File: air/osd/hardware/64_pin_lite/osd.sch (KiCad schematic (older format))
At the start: 0 parts

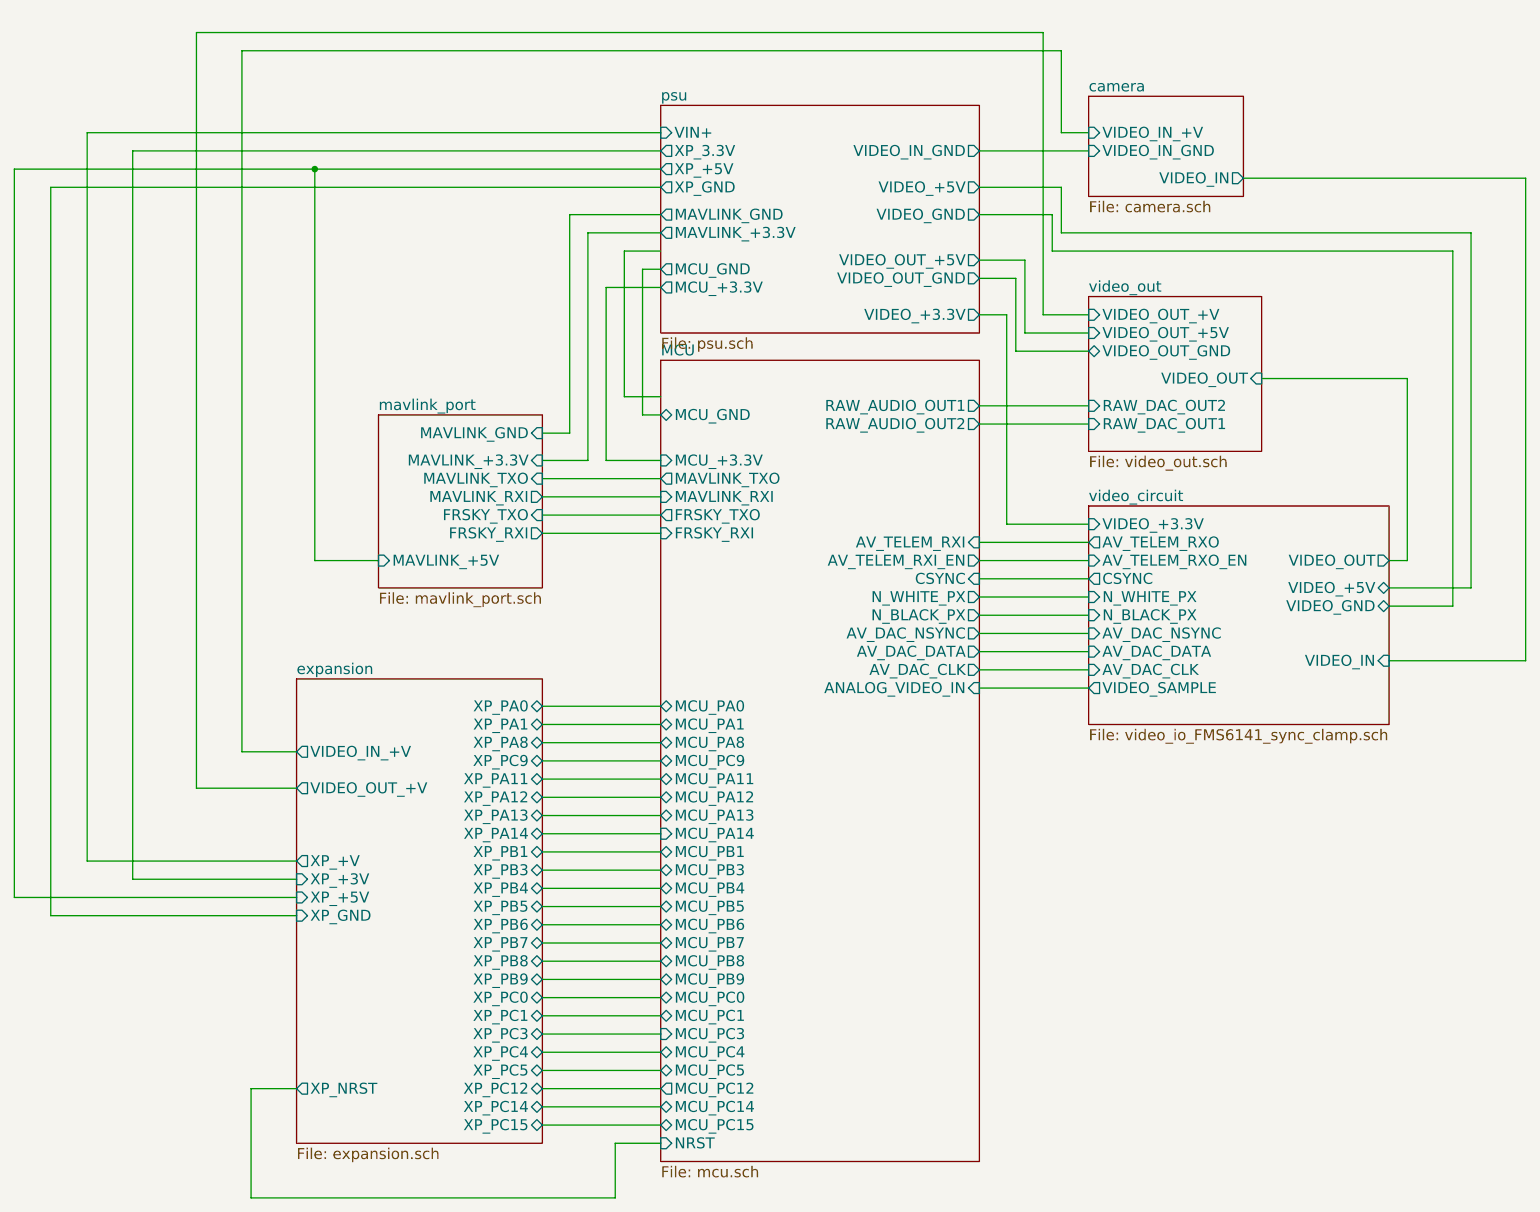
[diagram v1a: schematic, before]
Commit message: removed traces on pcb design. Added links to separate ground paths for modules. Moved mpu to other side of board. Added 2 pin power conector at end of board
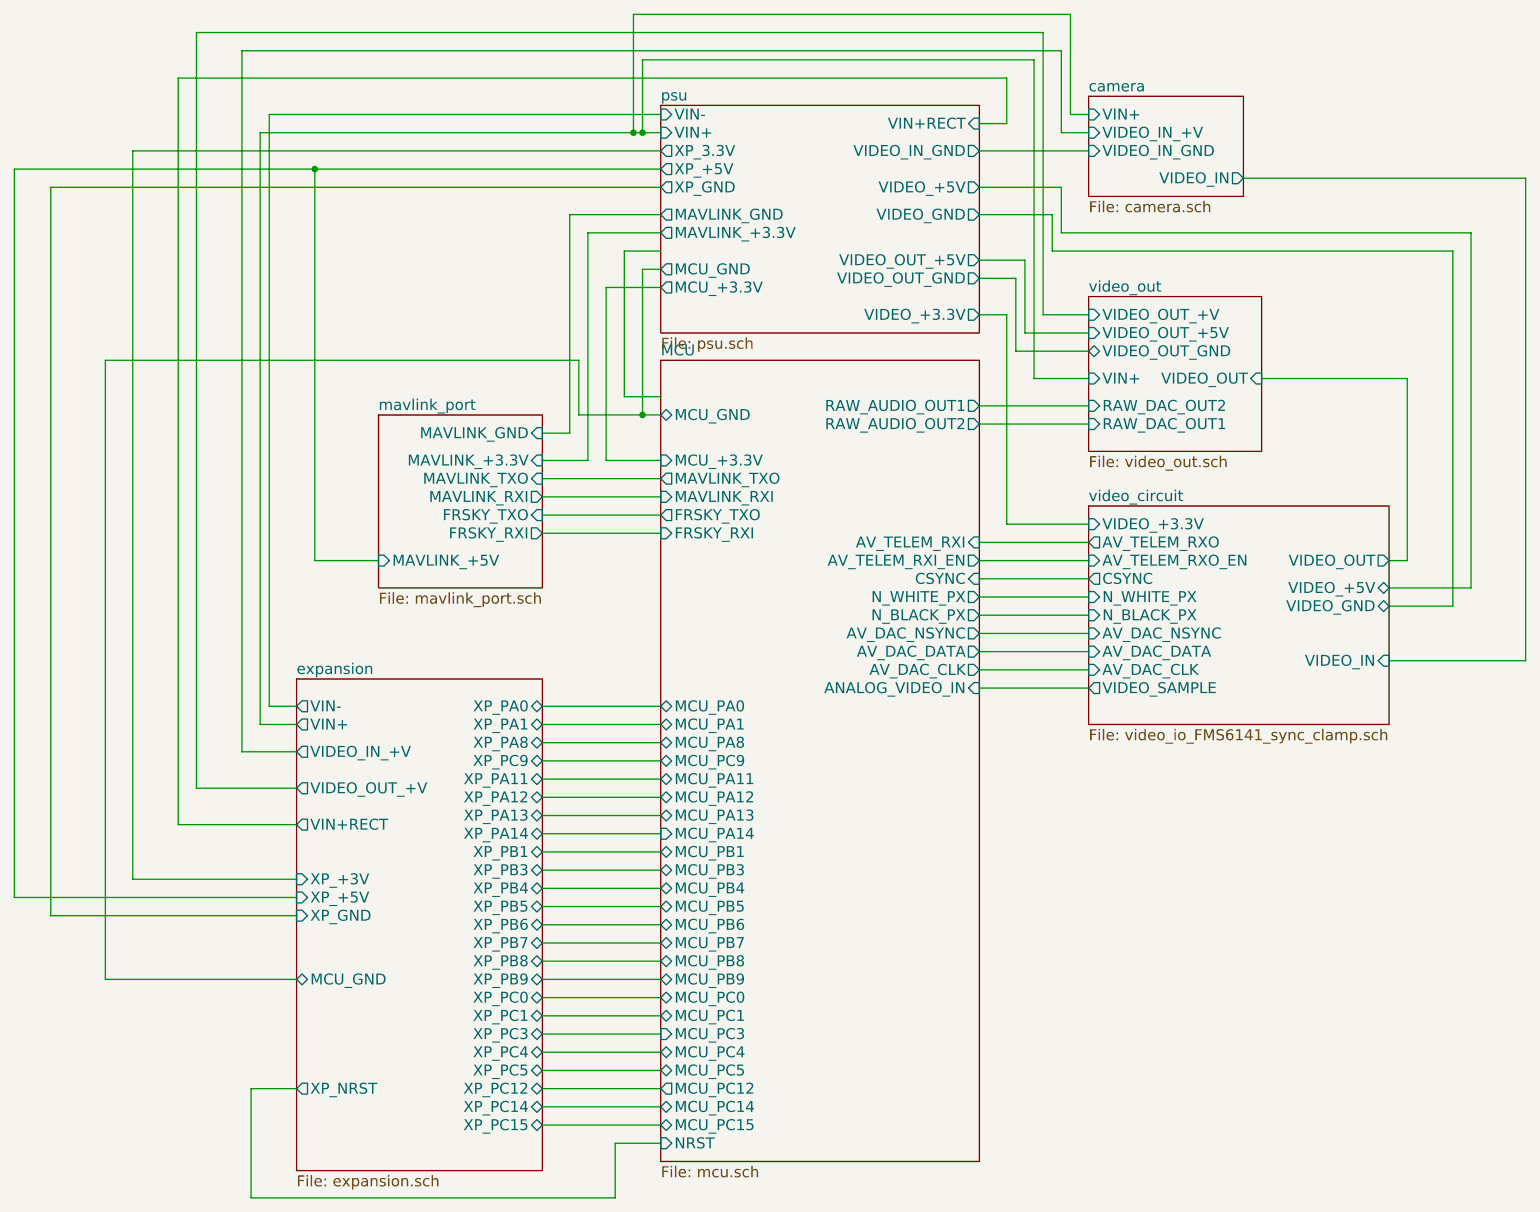
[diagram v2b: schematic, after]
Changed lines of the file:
@@
-EESchema Schematic File Version 2  date Mon 26 Jan 2015 12:32:55 GMT
+EESchema Schematic File Version 2  date Wed 04 Mar 2015 21:55:30 GMT
 LIBS:lm358
 LIBS:conn_6
@@
 LIBS:tlv3501
 LIBS:74lvc1g86
+LIBS:R0link
+LIBS:osd-cache
 EELAYER 25  0
 EELAYER END
@@
 Sheet 1 8
 Title ""
-Date "26 jan 2015"
+Date "4 mar 2015"
 Rev ""
 Comp ""
@@
 Comment4 ""
 $EndDescr
+Connection ~ 4600 1250
+Wire Wire Line
+	4600 1250 4600 850
+Wire Wire Line
+	4600 850  6750 850
+Wire Wire Line
+	6750 850  6750 2600
+Wire Wire Line
+	6750 2600 7050 2600
+Connection ~ 4600 2800
+Wire Wire Line
+	4700 2800 4250 2800
+Wire Wire Line
+	4250 2800 4250 2500
+Wire Wire Line
+	4250 2500 1650 2500
+Wire Wire Line
+	1650 2500 1650 5900
+Wire Wire Line
+	1650 5900 2700 5900
+Wire Wire Line
+	6450 1200 6600 1200
+Wire Wire Line
+	6600 1200 6600 950
+Wire Wire Line
+	6600 950  2050 950
+Wire Wire Line
+	2050 950  2050 5050
+Wire Wire Line
+	2050 5050 2700 5050
 Connection ~ 2800 1450
 Wire Wire Line
@@
 	4050 6700 4700 6700
 Wire Wire Line
-	4700 2800 4600 2800
-Wire Wire Line
 	4600 2800 4600 2000
 Wire Wire Line
@@
 	6450 2850 7050 2850
 Wire Wire Line
-	2700 5250 1550 5250
-Wire Wire Line
-	1550 5250 1550 1250
-Wire Wire Line
-	1550 1250 4700 1250
-Wire Wire Line
 	2700 4650 2400 4650
 Wire Wire Line
@@
 Wire Wire Line
 	4450 6800 4700 6800
+Wire Wire Line
+	2700 4400 2550 4400
+Wire Wire Line
+	2550 4400 2550 1150
+Wire Wire Line
+	2550 1150 4700 1150
+Wire Wire Line
+	2700 4500 2500 4500
+Wire Wire Line
+	2500 4500 2500 1250
+Wire Wire Line
+	2500 1250 4700 1250
+Wire Wire Line
+	7050 1150 6950 1150
+Wire Wire Line
+	6950 1150 6950 600
+Wire Wire Line
+	6950 600  4550 600
+Wire Wire Line
+	4550 600  4550 1250
+Connection ~ 4550 1250
 $Sheet
 S 4700 2500 1750 4400
@@
 F14 "MCU_+3.3V" O L 4700 2100 60
 F15 "XP_3.3V" O L 4700 1350 60
+F16 "VIN-" I L 4700 1150 60
+F17 "VIN+RECT" I R 6450 1200 60
 $EndSheet
 $Sheet
@@
 F3 "VIDEO_IN_GND" I L 7050 1350 60
 F4 "VIDEO_IN_+V" I L 7050 1250 60
-$EndSheet
-$Sheet
-S 2700 4250 1350 2550
+F5 "VIN+" I L 7050 1150 60
+$EndSheet
+$Sheet
+S 2700 4250 1350 2700
 U 546D98A5
 F0 "expansion" 60
@@
 F26 "XP_+5V" I L 2700 5450 60
 F27 "XP_PC12" B R 4050 6500 60
-F28 "XP_+V" O L 2700 5250 60
-F29 "XP_+3V" I L 2700 5350 60
-F30 "VIDEO_OUT_+V" O L 2700 4850 60
-F31 "VIDEO_IN_+V" O L 2700 4650 60
-F32 "XP_NRST" O L 2700 6500 60
+F28 "XP_+3V" I L 2700 5350 60
+F29 "VIDEO_OUT_+V" O L 2700 4850 60
+F30 "VIDEO_IN_+V" O L 2700 4650 60
+F31 "XP_NRST" O L 2700 6500 60
+F32 "VIN-" O L 2700 4400 60
+F33 "VIN+" O L 2700 4500 60
+F34 "VIN+RECT" O L 2700 5050 60
+F35 "MCU_GND" B L 2700 5900 60
 $EndSheet
 $Sheet
@@
 F6 "VIDEO_OUT_+5V" I L 7050 2350 60
 F7 "VIDEO_OUT_+V" I L 7050 2250 60
-$EndSheet
-$Sheet
+F8 "VIN+" I L 7050 2600 60
+$EndSheet
+$Sheet

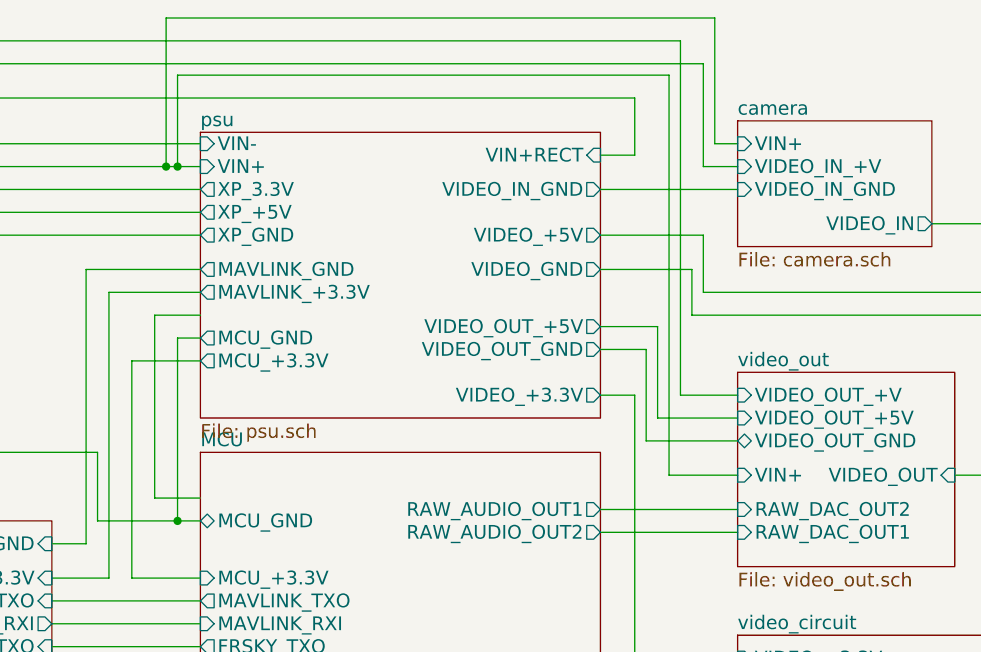
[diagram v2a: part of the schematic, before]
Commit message: laid out components on boar. No traces done yet
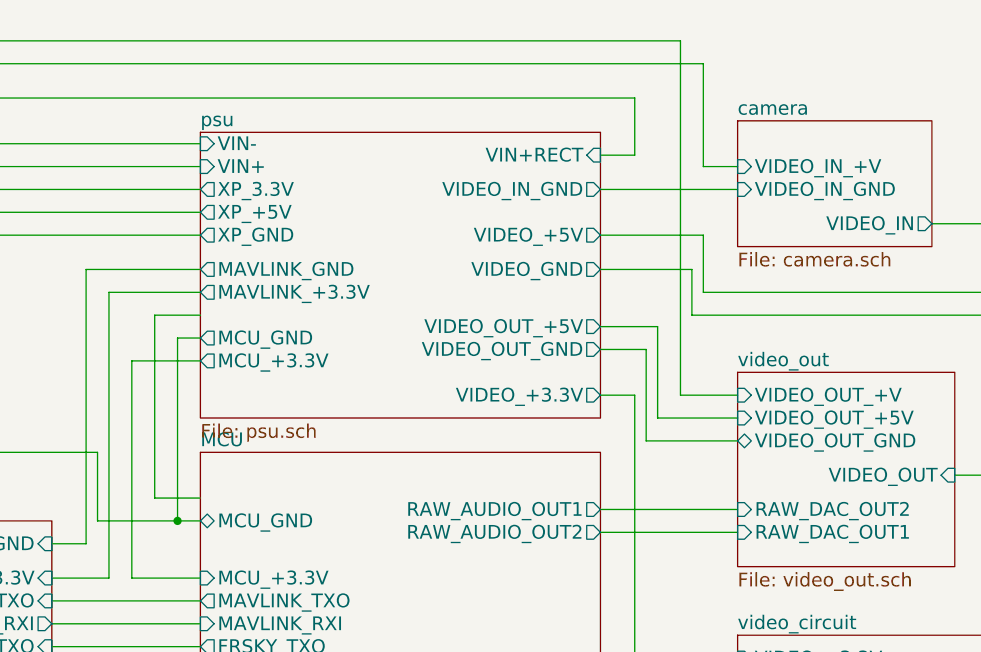
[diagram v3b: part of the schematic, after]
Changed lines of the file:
@@
-EESchema Schematic File Version 2  date Wed 04 Mar 2015 21:55:30 GMT
+EESchema Schematic File Version 2  date Thu 05 Mar 2015 23:13:03 GMT
 LIBS:lm358
 LIBS:conn_6
@@
 Sheet 1 8
 Title ""
-Date "4 mar 2015"
+Date "5 mar 2015"
 Rev ""
 Comp ""
@@
 Comment4 ""
 $EndDescr
-Connection ~ 4600 1250
-Wire Wire Line
-	4600 1250 4600 850
-Wire Wire Line
-	4600 850  6750 850
-Wire Wire Line
-	6750 850  6750 2600
-Wire Wire Line
-	6750 2600 7050 2600
+Wire Wire Line
+	2700 4500 2500 4500
+Wire Wire Line
+	2500 4500 2500 1250
+Wire Wire Line
+	2500 1250 4700 1250
 Connection ~ 4600 2800
 Wire Wire Line
@@
 Wire Wire Line
 	2550 1150 4700 1150
-Wire Wire Line
-	2700 4500 2500 4500
-Wire Wire Line
-	2500 4500 2500 1250
-Wire Wire Line
-	2500 1250 4700 1250
-Wire Wire Line
-	7050 1150 6950 1150
-Wire Wire Line
-	6950 1150 6950 600
-Wire Wire Line
-	6950 600  4550 600
-Wire Wire Line
-	4550 600  4550 1250
-Connection ~ 4550 1250
 $Sheet
 S 4700 2500 1750 4400
@@
 F3 "VIDEO_IN_GND" I L 7050 1350 60
 F4 "VIDEO_IN_+V" I L 7050 1250 60
-F5 "VIN+" I L 7050 1150 60
 $EndSheet
 $Sheet
@@
 F6 "VIDEO_OUT_+5V" I L 7050 2350 60
 F7 "VIDEO_OUT_+V" I L 7050 2250 60
-F8 "VIN+" I L 7050 2600 60
-$EndSheet
-$Sheet
+$EndSheet
+$Sheet

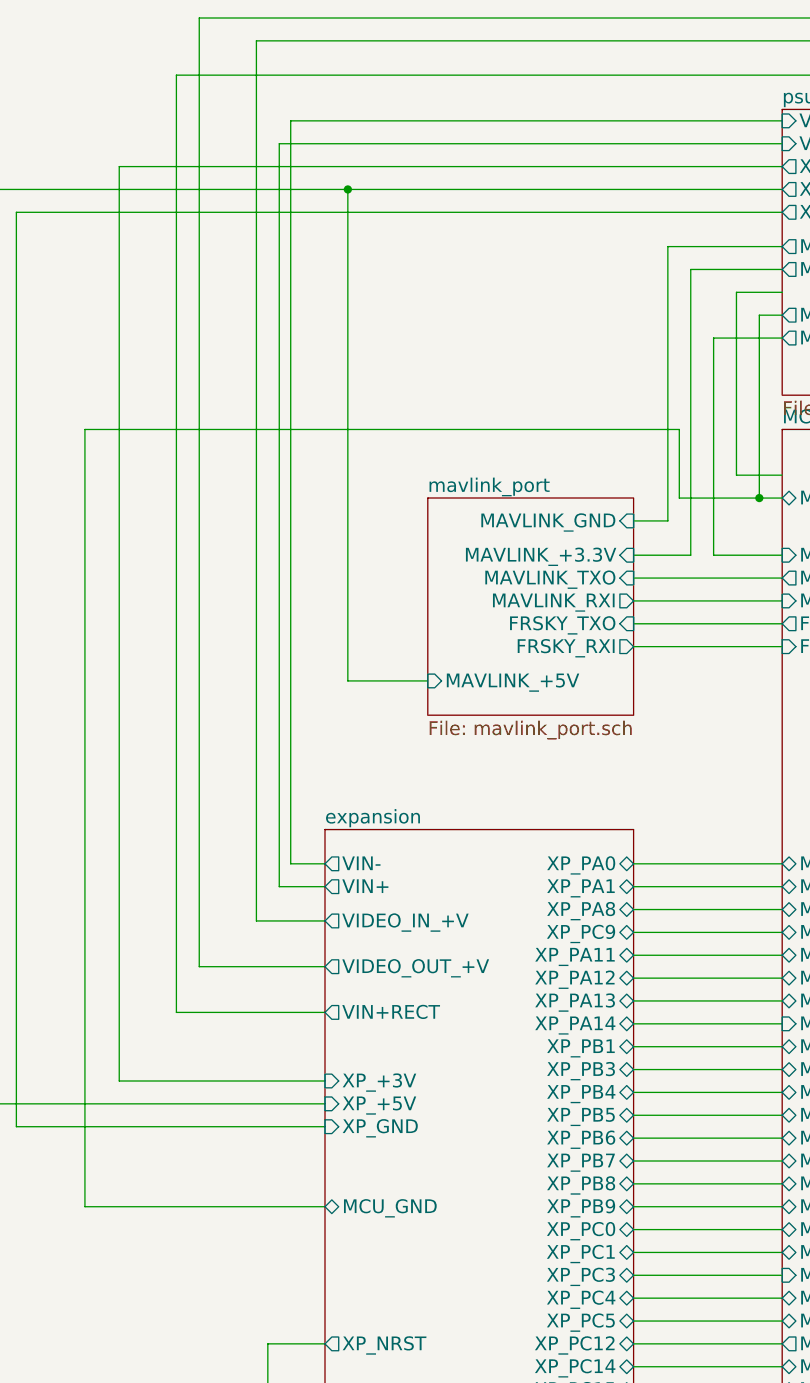
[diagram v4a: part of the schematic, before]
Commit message: moving pins around on expansion, but reckon I will get routing donr
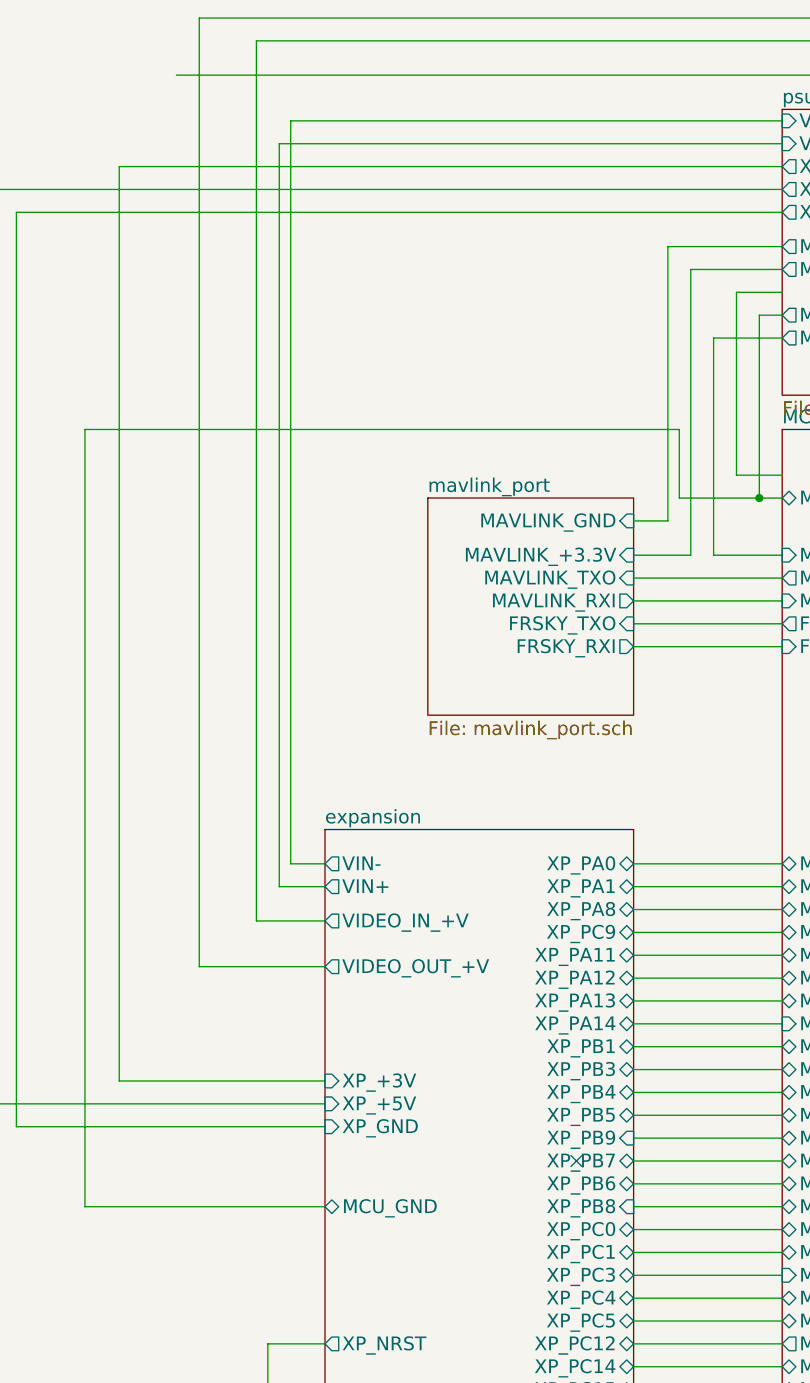
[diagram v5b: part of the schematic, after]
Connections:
- no-connect marks 0 -> 1
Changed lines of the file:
@@
-EESchema Schematic File Version 2  date Fri 06 Mar 2015 00:28:55 GMT
+EESchema Schematic File Version 2  date Sat 07 Mar 2015 18:05:27 GMT
 LIBS:lm358
 LIBS:conn_6
@@
 Sheet 1 8
 Title ""
-Date "6 mar 2015"
+Date "7 mar 2015"
 Rev ""
 Comp ""
@@
 Comment4 ""
 $EndDescr
+NoConn ~ 3800 5700
 Wire Wire Line
 	2700 4500 2500 4500
@@
 Wire Wire Line
 	6600 950  2050 950
-Wire Wire Line
-	2050 950  2050 5050
-Wire Wire Line
-	2050 5050 2700 5050
-Connection ~ 2800 1450
-Wire Wire Line
-	2800 1450 2800 3600
-Wire Wire Line
-	2800 3600 3150 3600
 Wire Wire Line
 	4700 2700 4500 2700
@@
 F9 "XP_PC1" B R 4050 6100 60
 F10 "XP_PC0" B R 4050 6000 60
-F11 "XP_PB9" B R 4050 5900 60
-F12 "XP_PB8" B R 4050 5800 60
-F13 "XP_PB7" B R 4050 5700 60
-F14 "XP_PB6" B R 4050 5600 60
-F15 "XP_PB5" B R 4050 5500 60
-F16 "XP_PB4" B R 4050 5400 60
-F17 "XP_PB3" B R 4050 5300 60
-F18 "XP_PB1" B R 4050 5200 60
-F19 "XP_PA14" B R 4050 5100 60
-F20 "XP_PA13" B R 4050 5000 60
-F21 "XP_PA12" B R 4050 4900 60
-F22 "XP_PA11" B R 4050 4800 60
-F23 "XP_PA8" B R 4050 4600 60
-F24 "XP_PA1" B R 4050 4500 60
-F25 "XP_PA0" B R 4050 4400 60
-F26 "XP_+5V" I L 2700 5450 60
-F27 "XP_PC12" B R 4050 6500 60
-F28 "XP_+3V" I L 2700 5350 60
-F29 "VIDEO_OUT_+V" O L 2700 4850 60
-F30 "VIDEO_IN_+V" O L 2700 4650 60
-F31 "XP_NRST" O L 2700 6500 60
-F32 "VIN-" O L 2700 4400 60
-F33 "VIN+" O L 2700 4500 60
-F34 "VIN+RECT" O L 2700 5050 60
-F35 "MCU_GND" B L 2700 5900 60
+F11 "XP_PB5" B R 4050 5500 60
+F12 "XP_PB4" B R 4050 5400 60
+F13 "XP_PB3" B R 4050 5300 60
+F14 "XP_PB1" B R 4050 5200 60
+F15 "XP_PA14" B R 4050 5100 60
+F16 "XP_PA13" B R 4050 5000 60
+F17 "XP_PA12" B R 4050 4900 60
+F18 "XP_PA11" B R 4050 4800 60
+F19 "XP_PA8" B R 4050 4600 60
+F20 "XP_PA1" B R 4050 4500 60
+F21 "XP_PA0" B R 4050 4400 60
+F22 "XP_+5V" I L 2700 5450 60
+F23 "XP_PC12" B R 4050 6500 60
+F24 "XP_+3V" I L 2700 5350 60
+F25 "VIDEO_OUT_+V" O L 2700 4850 60
+F26 "VIDEO_IN_+V" O L 2700 4650 60
+F27 "XP_NRST" O L 2700 6500 60
+F28 "VIN-" O L 2700 4400 60
+F29 "VIN+" O L 2700 4500 60
+F30 "MCU_GND" B L 2700 5900 60
+F31 "XP_PB9" I R 4050 5600 60
+F32 "XP_PB7" B R 4050 5700 60
+F33 "XP_PB6" B R 4050 5800 60
+F34 "XP_PB8" I R 4050 5900 60
 $EndSheet
 $Sheet
@@
 F6 "FRSKY_RXI" O R 4050 3450 60
 F7 "MAVLINK_+3.3V" I R 4050 3050 60
-F8 "MAVLINK_+5V" I L 3150 3600 60
 $EndSheet
 $Sheet
